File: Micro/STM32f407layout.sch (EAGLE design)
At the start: 41 parts, among them Q1 ASF, U1 LM1085IS-3.3

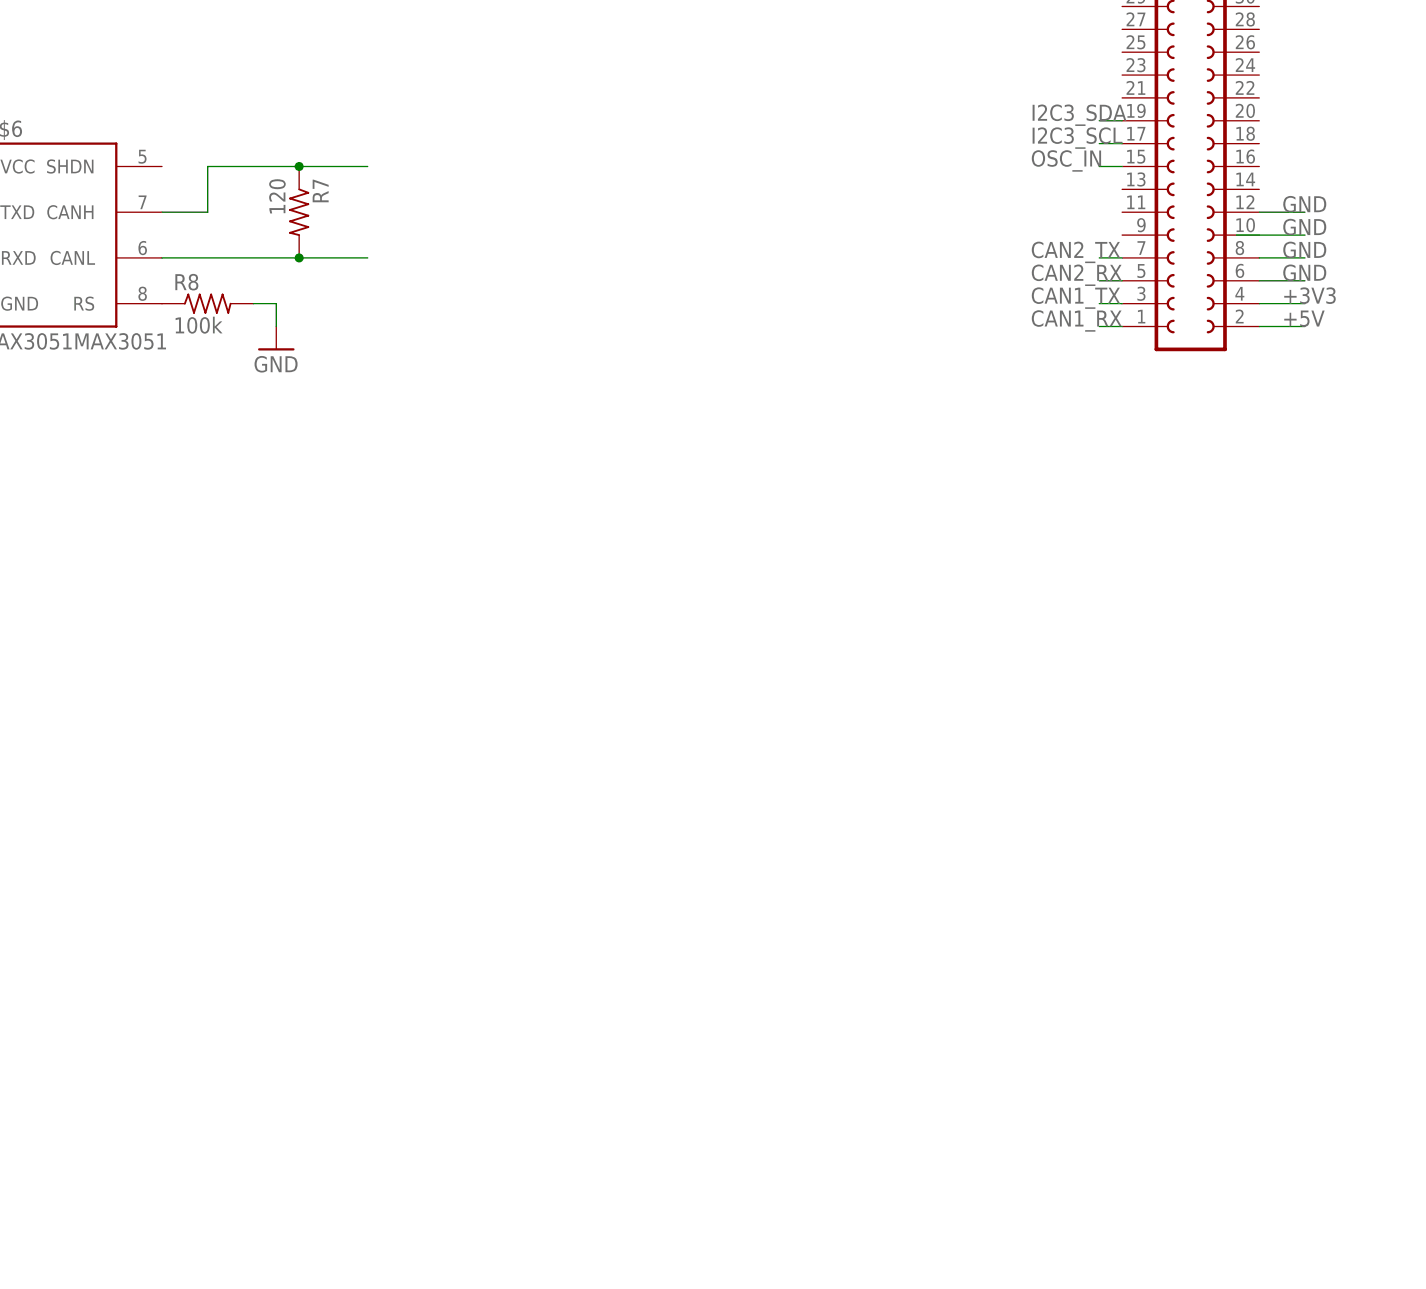
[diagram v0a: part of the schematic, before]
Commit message: worked on board layout, set initial width requirements
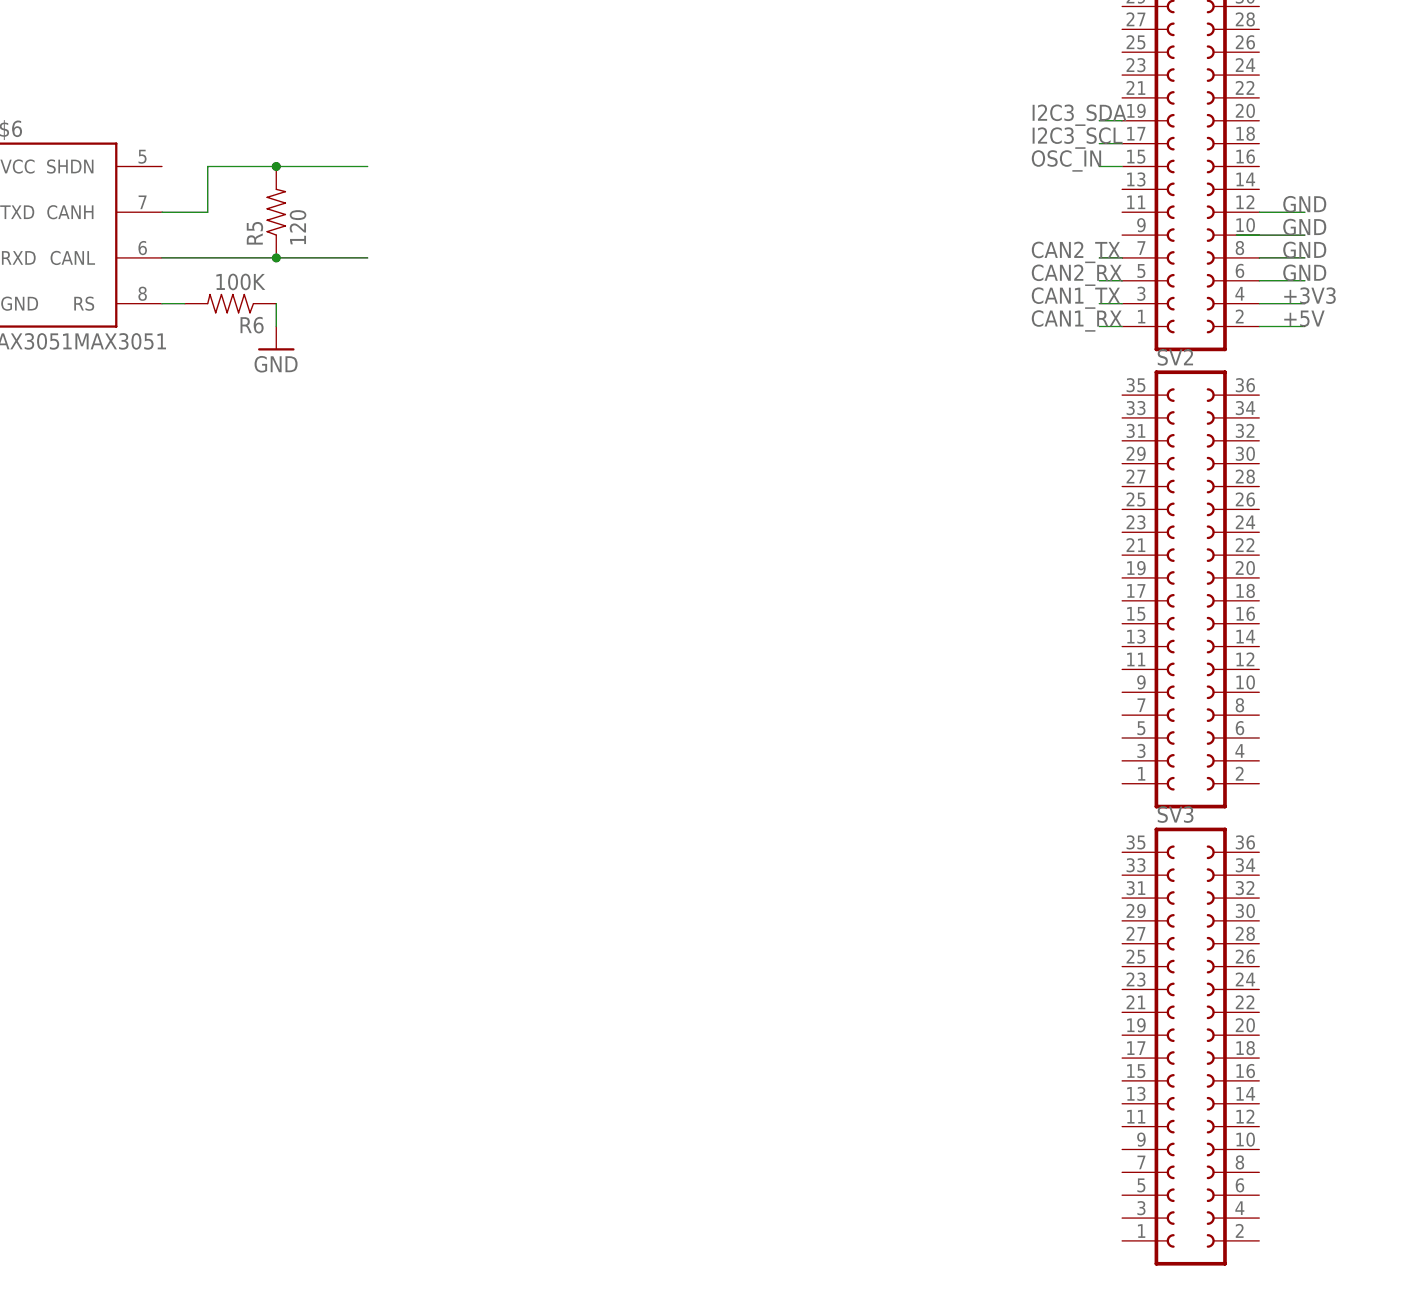
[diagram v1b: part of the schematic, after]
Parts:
- removed R7: 120, resistor:R-US_0204/2V
- removed R8: 100k, resistor:R-US_0204/2V
- added R5: 120, SparkFun-Passives:RESISTOR0603-RES
- added R6: 100K, SparkFun-Passives:RESISTOR0603-RES
- added SV2, SV3: (no value), Connectors:FE18-2
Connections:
- removed net N$13: R8.1, U$6.RS
- new net N$11: R6.2, U$6.RS
- net CANH1: now also R5.2; no longer R7.1
- net CANL1: now also R5.1; no longer R7.2
- net GND: now also R6.1; no longer R8.2
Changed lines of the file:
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@@
 <?xml version="1.0" encoding="utf-8"?>
 <!DOCTYPE eagle SYSTEM "eagle.dtd">
-<eagle version="7.5.0">
+<eagle version="7.4.0">
 <drawing>
 <settings>
@@
 <part name="U1" library="PowerComponents" deviceset="LM1085IS-3.3" device=""/>
 <part name="U$6" library="MAX3051 Library" deviceset="MAX3051" device="MAX3051"/>
-<part name="R7" library="resistor" deviceset="R-US_" device="0204/2V" value="120"/>
-<part name="R8" library="resistor" deviceset="R-US_" device="0204/2V" value="100k"/>
 <part name="SUPPLY2" library="SparkFun-Aesthetics" deviceset="VCC" device=""/>
 <part name="GND13" library="SparkFun-Aesthetics" deviceset="GND" device=""/>
@@
 <part name="C8" library="SparkFun-Passives" deviceset="CAP" device="0603-CAP" value="4.7uF"/>
 <part name="GND15" library="supply1" deviceset="GND" device=""/>
+<part name="SV2" library="Connectors" deviceset="FE18-2" device=""/>
+<part name="SV3" library="Connectors" deviceset="FE18-2" device=""/>
+<part name="R5" library="SparkFun-Passives" deviceset="RESISTOR" device="0603-RES" value="120"/>
+<part name="R6" library="SparkFun-Passives" deviceset="RESISTOR" device="0603-RES" value="100K"/>
 </parts>
 <sheets>
@@
 <instance part="U1" gate="A" x="91.44" y="147.32"/>
 <instance part="U$6" gate="G$1" x="543.56" y="215.9"/>
-<instance part="R7" gate="G$1" x="571.5" y="218.44" rot="R270"/>
-<instance part="R8" gate="G$1" x="561.34" y="208.28"/>
 <instance part="SUPPLY2" gate="G$1" x="525.78" y="226.06"/>
 <instance part="GND13" gate="1" x="525.78" y="203.2"/>
@@
 <instance part="C8" gate="G$1" x="309.88" y="353.06"/>
 <instance part="GND15" gate="1" x="175.26" y="378.46"/>
+<instance part="SV2" gate="G$1" x="670.56" y="177.8"/>
+<instance part="SV3" gate="G$1" x="670.56" y="127"/>
+<instance part="R5" gate="G$1" x="568.96" y="218.44" rot="R90"/>
+<instance part="R6" gate="G$1" x="563.88" y="208.28" rot="R180"/>
 </instances>
 <busses>
@@
 </segment>
 <segment>
-<pinref part="R8" gate="G$1" pin="2"/>
-<wire x1="566.42" y1="208.28" x2="568.96" y2="208.28" width="0.1524" layer="91"/>
 <wire x1="568.96" y1="208.28" x2="568.96" y2="205.74" width="0.1524" layer="91"/>
 <pinref part="GND14" gate="1" pin="GND"/>
+<pinref part="R6" gate="G$1" pin="1"/>
 </segment>
 <segment>
@@
 </segment>
 </net>
-<net name="N$13" class="0">
-<segment>
-<pinref part="U$6" gate="G$1" pin="RS"/>
-<pinref part="R8" gate="G$1" pin="1"/>
-</segment>
-</net>
 <net name="CANL1" class="0">
 <segment>
 <pinref part="U$6" gate="G$1" pin="CANL"/>
-<wire x1="556.26" y1="213.36" x2="571.5" y2="213.36" width="0.1524" layer="91"/>
-<pinref part="R7" gate="G$1" pin="2"/>
-<wire x1="571.5" y1="213.36" x2="579.12" y2="213.36" width="0.1524" layer="91"/>
-<junction x="571.5" y="213.36"/>
+<wire x1="556.26" y1="213.36" x2="568.96" y2="213.36" width="0.1524" layer="91"/>
+<pinref part="R5" gate="G$1" pin="1"/>
+<wire x1="568.96" y1="213.36" x2="579.12" y2="213.36" width="0.1524" layer="91"/>
+<junction x="568.96" y="213.36"/>
 </segment>
 </net>
 <net name="CANH1" class="0">
 <segment>
-<pinref part="R7" gate="G$1" pin="1"/>
-<wire x1="571.5" y1="223.52" x2="561.34" y2="223.52" width="0.1524" layer="91"/>
+<wire x1="579.12" y1="223.52" x2="568.96" y2="223.52" width="0.1524" layer="91"/>
+<wire x1="568.96" y1="223.52" x2="561.34" y2="223.52" width="0.1524" layer="91"/>
 <wire x1="561.34" y1="223.52" x2="561.34" y2="218.44" width="0.1524" layer="91"/>
 <pinref part="U$6" gate="G$1" pin="CANH"/>
 <wire x1="561.34" y1="218.44" x2="556.26" y2="218.44" width="0.1524" layer="91"/>
-<wire x1="571.5" y1="223.52" x2="579.12" y2="223.52" width="0.1524" layer="91"/>
-<junction x="571.5" y="223.52"/>
+<pinref part="R5" gate="G$1" pin="2"/>
+<junction x="568.96" y="223.52"/>
 </segment>
 </net>
@@
 </segment>
 </net>
+<net name="N$11" class="0">
+<segment>
+<pinref part="U$6" gate="G$1" pin="RS"/>
+<pinref part="R6" gate="G$1" pin="2"/>
+<wire x1="558.8" y1="208.28" x2="556.26" y2="208.28" width="0.1524" layer="91"/>
+</segment>
+</net>

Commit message: Updated Board
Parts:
- removed SV1, SV2, SV3: (no value), Connectors:FE18-2
- added R7: 4.7K, SparkFun-Passives:RESISTOR0603-RES
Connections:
- removed net CAN1_RX: SV1.1
- removed net CAN1_TX: SV1.3
- new net TEMP_SENSE_INFO: R7.1, U$1G$4.PD0
- net +3V3: now also R7.2; no longer SV1.4
- net +5V: no longer SV1.2
- net CAN2_RX: no longer SV1.5
- net CAN2_TX: no longer SV1.7
- net GND: no longer SV1.12, SV1.6, SV1.8
- net I2C1_SCL: no longer SV1.33
- net I2C1_SDA: no longer SV1.35
- net I2C3_SCL: no longer SV1.17
- net I2C3_SDA: no longer SV1.19
- net OSC_IN: no longer SV1.15
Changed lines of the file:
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@@
 <part name="D5" library="SparkFun-LED" deviceset="LED" device="0603"/>
 <part name="GND16" library="SparkFun-Aesthetics" deviceset="GND" device=""/>
-<part name="SV1" library="Connectors" deviceset="FE18-2" device=""/>
 <part name="GND17" library="SparkFun-Aesthetics" deviceset="GND" device=""/>
 <part name="+3V8" library="supply1" deviceset="+3V3" device=""/>
@@
 <part name="C8" library="SparkFun-Passives" deviceset="CAP" device="0603-CAP" value="4.7uF"/>
 <part name="GND15" library="supply1" deviceset="GND" device=""/>
-<part name="SV2" library="Connectors" deviceset="FE18-2" device=""/>
-<part name="SV3" library="Connectors" deviceset="FE18-2" device=""/>
 <part name="R5" library="SparkFun-Passives" deviceset="RESISTOR" device="0603-RES" value="120"/>
 <part name="R6" library="SparkFun-Passives" deviceset="RESISTOR" device="0603-RES" value="100K"/>
+<part name="R7" library="SparkFun-Passives" deviceset="RESISTOR" device="0603-RES" value="4.7K"/>
+<part name="+3V11" library="supply1" deviceset="+3V3" device=""/>
 </parts>
 <sheets>
@@
 <instance part="D5" gate="G$1" x="604.52" y="276.86" rot="R90"/>
 <instance part="GND16" gate="1" x="617.22" y="269.24"/>
-<instance part="SV1" gate="G$1" x="670.56" y="228.6"/>
 <instance part="GND17" gate="1" x="68.58" y="134.62"/>
 <instance part="+3V8" gate="G$1" x="116.84" y="154.94"/>
@@
 <instance part="C8" gate="G$1" x="309.88" y="353.06"/>
 <instance part="GND15" gate="1" x="175.26" y="378.46"/>
-<instance part="SV2" gate="G$1" x="670.56" y="177.8"/>
-<instance part="SV3" gate="G$1" x="670.56" y="127"/>
 <instance part="R5" gate="G$1" x="568.96" y="218.44" rot="R90"/>
 <instance part="R6" gate="G$1" x="563.88" y="208.28" rot="R180"/>
+<instance part="R7" gate="G$1" x="614.68" y="353.06" rot="R90"/>
+<instance part="+3V11" gate="G$1" x="614.68" y="363.22"/>
 </instances>
 <busses>
@@
 </segment>
 <segment>
-<pinref part="SV1" gate="G$1" pin="6"/>
 <wire x1="678.18" y1="210.82" x2="683.26" y2="210.82" width="0.1524" layer="91"/>
 <label x="680.72" y="210.82" size="1.778" layer="95"/>
 </segment>
 <segment>
-<pinref part="SV1" gate="G$1" pin="8"/>
 <wire x1="678.18" y1="213.36" x2="683.26" y2="213.36" width="0.1524" layer="91"/>
 <label x="680.72" y="213.36" size="1.778" layer="95"/>
@@
 </segment>
 <segment>
-<pinref part="SV1" gate="G$1" pin="12"/>
 <wire x1="678.18" y1="218.44" x2="683.26" y2="218.44" width="0.1524" layer="91"/>
 <label x="680.72" y="218.44" size="1.778" layer="95"/>
@@
 </segment>
 <segment>
-<pinref part="SV1" gate="G$1" pin="4"/>
 <wire x1="678.18" y1="208.28" x2="683.26" y2="208.28" width="0.1524" layer="91"/>
 <label x="680.72" y="208.28" size="1.778" layer="95"/>
@@
 <junction x="416.306" y="242.57"/>
 </segment>
+<segment>
+<pinref part="R7" gate="G$1" pin="2"/>
+<pinref part="+3V11" gate="G$1" pin="+3V3"/>
+<wire x1="614.68" y1="358.14" x2="614.68" y2="360.68" width="0.1524" layer="91"/>
+</segment>
 </net>
 <net name="N$3" class="0">
@@
 </segment>
 <segment>
-<pinref part="SV1" gate="G$1" pin="17"/>
 <wire x1="662.94" y1="226.06" x2="660.4" y2="226.06" width="0.1524" layer="91"/>
 <label x="652.78" y="226.06" size="1.778" layer="95"/>
@@
 </segment>
 <segment>
-<pinref part="SV1" gate="G$1" pin="19"/>
 <wire x1="662.94" y1="228.6" x2="660.4" y2="228.6" width="0.1524" layer="91"/>
 <label x="652.78" y="228.6" size="1.778" layer="95"/>
@@
 </segment>
 <segment>
-<pinref part="SV1" gate="G$1" pin="2"/>
 <wire x1="678.18" y1="205.74" x2="683.26" y2="205.74" width="0.1524" layer="91"/>
 <label x="680.72" y="205.74" size="1.778" layer="95"/>
@@
 </segment>
 <segment>
-<pinref part="SV1" gate="G$1" pin="15"/>
 <wire x1="662.94" y1="223.52" x2="660.4" y2="223.52" width="0.1524" layer="91"/>
 <label x="652.78" y="223.52" size="1.778" layer="95"/>
@@
 <net name="CAN1_TX" class="0">
 <segment>
-<pinref part="SV1" gate="G$1" pin="3"/>
 <wire x1="662.94" y1="208.28" x2="660.4" y2="208.28" width="0.1524" layer="91"/>
 <label x="652.78" y="208.28" size="1.778" layer="95"/>
@@
 <net name="CAN2_TX" class="0">
 <segment>
-<pinref part="SV1" gate="G$1" pin="7"/>
 <wire x1="662.94" y1="213.36" x2="660.4" y2="213.36" width="0.1524" layer="91"/>
 <label x="652.78" y="213.36" size="1.778" layer="95"/>
@@
 </segment>
 <segment>
-<pinref part="SV1" gate="G$1" pin="5"/>
 <wire x1="662.94" y1="210.82" x2="660.4" y2="210.82" width="0.1524" layer="91"/>
 <label x="652.78" y="210.82" size="1.778" layer="95"/>
@@
 <net name="CAN1_RX" class="0">
 <segment>
-<pinref part="SV1" gate="G$1" pin="1"/>
 <wire x1="662.94" y1="205.74" x2="660.4" y2="205.74" width="0.1524" layer="91"/>
 <label x="652.78" y="205.74" size="1.778" layer="95"/>
@@
 </segment>
 <segment>
-<pinref part="SV1" gate="G$1" pin="35"/>
 <wire x1="662.94" y1="248.92" x2="660.4" y2="248.92" width="0.1524" layer="91"/>
 <label x="650.24" y="248.92" size="1.778" layer="95"/>
@@
 </segment>
 <segment>
-<pinref part="SV1" gate="G$1" pin="33"/>
 <wire x1="662.94" y1="246.38" x2="660.4" y2="246.38" width="0.1524" layer="91"/>
 <label x="650.24" y="246.38" size="1.778" layer="95"/>
@@
 </segment>
 </net>
+<net name="TEMP_SENSE_INFO" class="0">
+<segment>
+<pinref part="U$1" gate="G$4" pin="PD0"/>
+<wire x1="586.74" y1="347.98" x2="614.68" y2="347.98" width="0.1524" layer="91"/>
+<label x="589.28" y="347.98" size="1.778" layer="95"/>
+<pinref part="R7" gate="G$1" pin="1"/>
+<wire x1="614.68" y1="347.98" x2="619.76" y2="347.98" width="0.1524" layer="91"/>
+<junction x="614.68" y="347.98"/>
+</segment>
+</net>

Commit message: More Board Updates
Remind myself to switch LED pins
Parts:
- removed R7: 4.7K, SparkFun-Passives:RESISTOR0603-RES
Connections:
- removed net CAN2_RX: U$1G$2.PB5
- removed net CAN2_TX: U$1G$2.PB6
- removed net TEMP_SENSE_INFO: R7.1, U$1G$4.PD0
- net +3V3: no longer R7.2
- net CAN_RX: now also U$1G$2.PB5
- net CAN_TX: now also U$1G$2.PB6
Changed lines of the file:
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@@
 <part name="R5" library="SparkFun-Passives" deviceset="RESISTOR" device="0603-RES" value="120"/>
 <part name="R6" library="SparkFun-Passives" deviceset="RESISTOR" device="0603-RES" value="100K"/>
-<part name="R7" library="SparkFun-Passives" deviceset="RESISTOR" device="0603-RES" value="4.7K"/>
-<part name="+3V11" library="supply1" deviceset="+3V3" device=""/>
 </parts>
 <sheets>
@@
 <instance part="R5" gate="G$1" x="568.96" y="218.44" rot="R90"/>
 <instance part="R6" gate="G$1" x="563.88" y="208.28" rot="R180"/>
-<instance part="R7" gate="G$1" x="614.68" y="353.06" rot="R90"/>
-<instance part="+3V11" gate="G$1" x="614.68" y="363.22"/>
 </instances>
 <busses>
@@
 <junction x="416.306" y="242.57"/>
 </segment>
-<segment>
-<pinref part="R7" gate="G$1" pin="2"/>
-<pinref part="+3V11" gate="G$1" pin="+3V3"/>
-<wire x1="614.68" y1="358.14" x2="614.68" y2="360.68" width="0.1524" layer="91"/>
-</segment>
 </net>
 <net name="N$3" class="0">
@@
 <label x="652.78" y="213.36" size="1.778" layer="95"/>
 </segment>
-<segment>
-<pinref part="U$1" gate="G$2" pin="PB6"/>
-<wire x1="439.42" y1="322.58" x2="454.66" y2="322.58" width="0.1524" layer="91"/>
-<label x="449.58" y="322.58" size="1.778" layer="95"/>
-</segment>
 </net>
 <net name="CAN2_RX" class="0">
-<segment>
-<pinref part="U$1" gate="G$2" pin="PB5"/>
-<wire x1="439.42" y1="327.66" x2="454.66" y2="327.66" width="0.1524" layer="91"/>
-<label x="449.58" y="327.66" size="1.778" layer="95"/>
-</segment>
 <segment>
 <wire x1="662.94" y1="210.82" x2="660.4" y2="210.82" width="0.1524" layer="91"/>
@@
 <label x="520.7" y="218.44" size="1.778" layer="95"/>
 </segment>
+<segment>
+<pinref part="U$1" gate="G$2" pin="PB6"/>
+<wire x1="439.42" y1="322.58" x2="454.66" y2="322.58" width="0.1524" layer="91"/>
+<label x="449.58" y="322.58" size="1.778" layer="95"/>
+</segment>
 </net>
 <net name="CAN_RX" class="0">
@@
 <label x="520.7" y="213.36" size="1.778" layer="95"/>
 </segment>
+<segment>
+<pinref part="U$1" gate="G$2" pin="PB5"/>
+<wire x1="439.42" y1="327.66" x2="454.66" y2="327.66" width="0.1524" layer="91"/>
+<label x="449.58" y="327.66" size="1.778" layer="95"/>
+</segment>
 </net>
 <net name="N$11" class="0">
@@
 </segment>
 </net>
-<net name="TEMP_SENSE_INFO" class="0">
-<segment>
-<pinref part="U$1" gate="G$4" pin="PD0"/>
-<wire x1="586.74" y1="347.98" x2="614.68" y2="347.98" width="0.1524" layer="91"/>
-<label x="589.28" y="347.98" size="1.778" layer="95"/>
-<pinref part="R7" gate="G$1" pin="1"/>
-<wire x1="614.68" y1="347.98" x2="619.76" y2="347.98" width="0.1524" layer="91"/>
-<junction x="614.68" y="347.98"/>
-</segment>
-</net>
